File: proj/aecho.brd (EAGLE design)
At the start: 43.2 x 24.6 mm, 47 parts, among them J3 SJ1-3523N, P1 I2C(SCL-SDA), P2 MP3_CTL(SCKR-SDI-DREQ-RST), P3 AMP_CTL(SHDN-CLK-UPDN), P4 PWR(GND-VIN-GND), P9 AOUT_L-GND-AOUT_R, U10 CS4334, U11 LM4811PDSO-10, U12 5.0V, U7 3.3V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

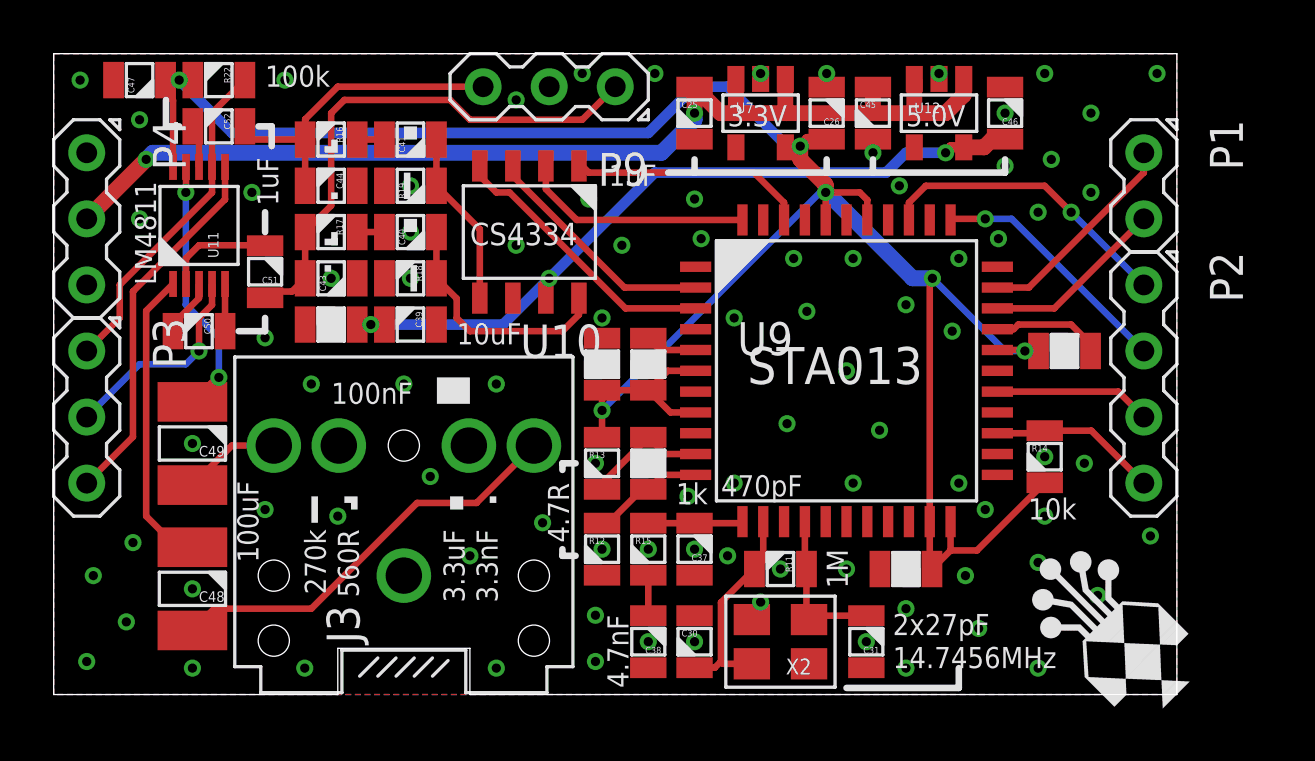
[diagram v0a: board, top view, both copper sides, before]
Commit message: @open #9 @open #4 @close #4 Exposed STA013 BIT_EN line in Aecho module
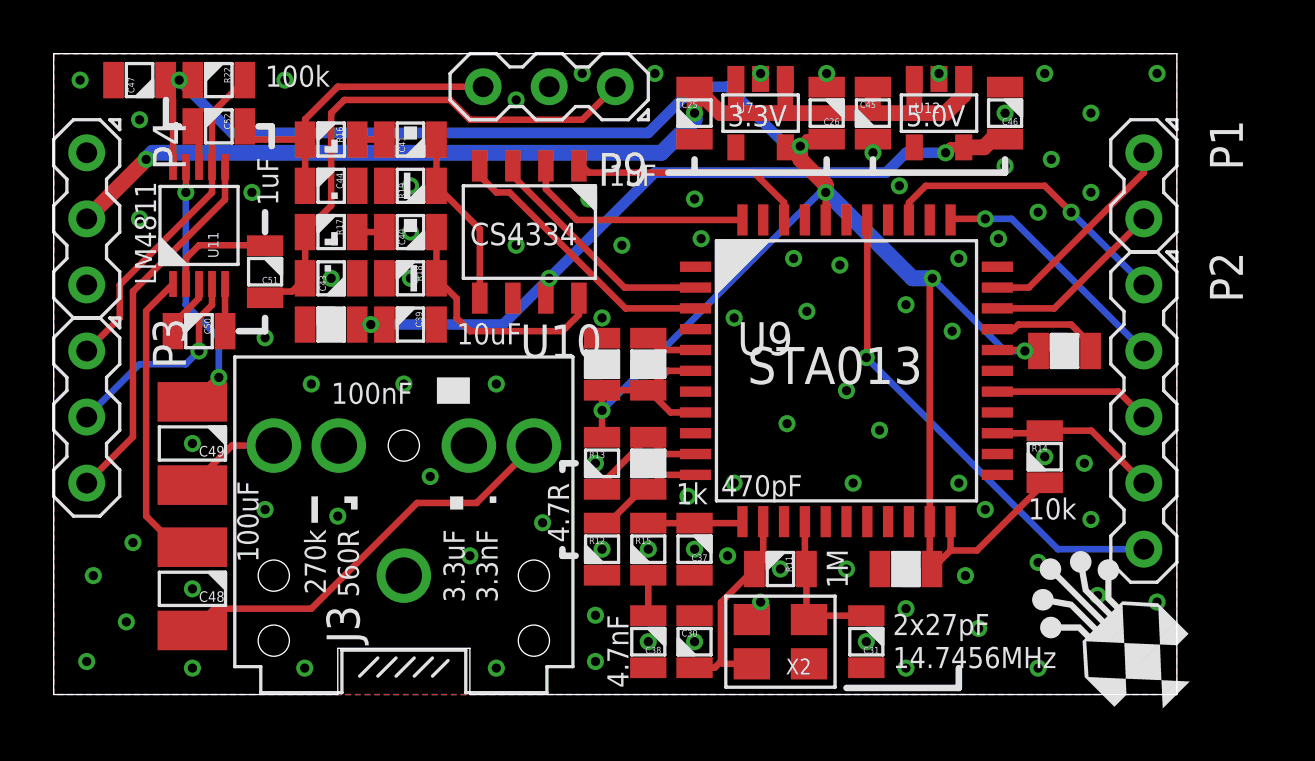
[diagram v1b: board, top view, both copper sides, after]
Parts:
- P2: device dooba:PIN_4 -> dooba:PIN_5
- moved P2 1.27 mm to (61.0, 27.9)
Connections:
- new net STA013_BIT_EN: P2.5, U9.38
- net 3.3V: no longer U9.38
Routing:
- net STA013_BIT_EN: track 0.00 -> 19.0 mm, vias 0 -> 1
- net 3.3V: track 88.7 -> 86.2 mm
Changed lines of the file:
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@@
 <setting verticaltext="up"/>
 </settings>
-<grid distance="1" unitdist="mil" unit="mil" style="lines" multiple="1" display="yes" altdistance="0.025" altunitdist="inch" altunit="inch"/>
+<grid distance="0.005" unitdist="inch" unit="inch" style="lines" multiple="1" display="yes" altdistance="0.025" altunitdist="inch" altunit="inch"/>
 <layers>
 <layer number="1" name="Top" color="4" fill="1" visible="yes" active="yes"/>
@@
 <layer number="23" name="tOrigins" color="15" fill="1" visible="yes" active="yes"/>
 <layer number="24" name="bOrigins" color="15" fill="1" visible="yes" active="yes"/>
-<layer number="25" name="tNames" color="7" fill="1" visible="no" active="yes"/>
+<layer number="25" name="tNames" color="7" fill="1" visible="yes" active="yes"/>
 <layer number="26" name="bNames" color="7" fill="1" visible="no" active="yes"/>
 <layer number="27" name="tValues" color="7" fill="1" visible="no" active="yes"/>
@@
 <layer number="115" name="ReferenceISLANDS" color="7" fill="1" visible="yes" active="yes"/>
 <layer number="116" name="Patch_BOT" color="9" fill="4" visible="yes" active="yes"/>
+<layer number="117" name="Refs" color="11" fill="1" visible="yes" active="yes"/>
 <layer number="118" name="Rect_Pads" color="7" fill="1" visible="yes" active="yes"/>
 <layer number="121" name="_tsilk" color="7" fill="1" visible="yes" active="yes"/>
@@
 <element name="X2" library="dooba" package="XTAL_3225" value="14.7456MHz" x="46.99" y="19.304" rot="R180"/>
 <element name="P1" library="dooba" package="PIN_2" value="I2C(SCL-SDA)" x="60.96" y="36.83" rot="R270"/>
-<element name="P2" library="dooba" package="PIN_4" value="MP3_CTL(SCKR-SDI-DREQ-RST)" x="60.96" y="29.21" rot="R270"/>
+<element name="P2" library="dooba" package="PIN_5" value="MP3_CTL(SCKR-SDI-DREQ-RST)" x="60.96" y="27.94" rot="R270"/>
 <element name="P3" library="dooba" package="PIN_3" value="AMP_CTL(SHDN-CLK-UPDN)" x="20.32" y="27.94" rot="R270"/>
 <element name="P4" library="dooba" package="PIN_3" value="PWR(GND-VIN-GND)" x="20.32" y="35.56" rot="R270"/>
@@
 <via x="51.816" y="18.288" extent="1-16" drill="0.3556"/>
 <via x="61.214" y="18.288" extent="1-16" drill="0.3556"/>
-<via x="61.214" y="23.368" extent="1-16" drill="0.3556"/>
+<via x="61.468" y="20.828" extent="1-16" drill="0.3556"/>
 <via x="58.674" y="26.162" extent="1-16" drill="0.3556"/>
 <via x="57.15" y="26.416" extent="1-16" drill="0.3556"/>
 <via x="54.102" y="21.844" extent="1-16" drill="0.3556"/>
-<via x="57.15" y="24.13" extent="1-16" drill="0.3556"/>
+<via x="58.928" y="24.003" extent="1-16" drill="0.3556"/>
 <via x="56.896" y="18.288" extent="1-16" drill="0.3556"/>
 <via x="54.61" y="19.812" extent="1-16" drill="0.3556"/>
@@
 <via x="53.848" y="25.4" extent="1-16" drill="0.3556"/>
 <via x="53.848" y="34.036" extent="1-16" drill="0.3556"/>
-<via x="49.784" y="34.036" extent="1-16" drill="0.3556"/>
+<via x="49.276" y="33.782" extent="1-16" drill="0.3556"/>
 <via x="51.816" y="32.258" extent="1-16" drill="0.3556"/>
 <via x="53.594" y="31.242" extent="1-16" drill="0.3556"/>
 <via x="49.784" y="25.4" extent="1-16" drill="0.3556"/>
-<via x="49.53" y="29.718" extent="1-16" drill="0.3556"/>
+<via x="49.53" y="28.956" extent="1-16" drill="0.3556"/>
 <via x="47.244" y="27.686" extent="1-16" drill="0.3556"/>
 <via x="48.006" y="32.004" extent="1-16" drill="0.3556"/>
@@
 <contactref element="U7" pad="5"/>
 <contactref element="U9" pad="40"/>
-<contactref element="U9" pad="38"/>
 <contactref element="U9" pad="29"/>
 <contactref element="C33" pad="2"/>
@@
 <wire x1="48.514" y1="36.576" x2="48.73" y2="36.576" width="0.254" layer="16"/>
 <via x="48.73" y="36.576" extent="1-16" drill="0.3556"/>
-<wire x1="50.33" y1="35.518" x2="50.33" y2="36.284" width="0.254" layer="1"/>
-<wire x1="50.33" y1="36.284" x2="50.038" y2="36.576" width="0.254" layer="1"/>
-<wire x1="50.038" y1="36.576" x2="48.73" y2="36.576" width="0.254" layer="1"/>
 <wire x1="47.752" y1="38.354" x2="47.752" y2="37.846" width="0.6096" layer="1"/>
 <wire x1="47.752" y1="37.846" x2="48.73" y2="36.868" width="0.6096" layer="1"/>
@@
 <wire x1="35.306" y1="24.638" x2="37.512" y2="26.844" width="0.254" layer="1"/>
 </signal>
+<signal name="STA013_BIT_EN">
+<contactref element="U9" pad="38"/>
+<contactref element="P2" pad="5"/>
+<wire x1="50.33" y1="35.518" x2="50.33" y2="30.264" width="0.254" layer="1"/>
+<wire x1="50.33" y1="30.264" x2="50.292" y2="30.226" width="0.254" layer="1"/>
+<via x="50.292" y="30.226" extent="1-16" drill="0.3556"/>
+<wire x1="50.292" y1="30.226" x2="57.658" y2="22.86" width="0.254" layer="16"/>
+<wire x1="57.658" y1="22.86" x2="60.96" y2="22.86" width="0.254" layer="16"/>
+</signal>
 </signals>
